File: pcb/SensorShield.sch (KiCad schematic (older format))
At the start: 51 parts, among them U14 ICE40UP5K-SG48ITR, U15 W25Q32JVSSIM

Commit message: stepper planes
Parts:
- removed R2: JUMPER, vs:ShortedJumper-2_P1.3mm_Bridged_Pad1.0x1.0mm, symbol UPduino_v3.0:Device_R
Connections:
- wire segments 327 -> 326
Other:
- note removed: "Core current \nmeasurement"
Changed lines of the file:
@@
 Wire Wire Line
 	2850 1900 3550 1900
-Text Label 4100 8350 0    50   ~ 0
+Text Label 4550 8350 2    50   ~ 0
 FLASH_MISO
 Text Label 5750 8550 0    50   ~ 0
@@
 Text Label 5750 8650 0    50   ~ 0
 IOB_25B_G3
-Text Label 4100 8250 0    50   ~ 0
+Text Label 4550 8250 2    50   ~ 0
 FLASH_MOSI
 $Comp
@@
 $EndComp
 $Comp
-L UPduino_v3.0:Device_R R?
-U 1 1 5E9D8BAA
-P 1100 6300
-AR Path="/5E9B245C/5E9D8BAA" Ref="R?"  Part="1"
-AR Path="/5E98CC69/5E9ECB99/5E9D8BAA" Ref="R2"  Part="1"
-AR Path="/5E9C016D/5E9D8BAA" Ref="R2"  Part="1"
-F 0 "R2" V 893 6300 50  0000 C CNN
-F 1 "JUMPER" V 984 6300 50  0000 C CNN
-F 2 "vs:ShortedJumper-2_P1.3mm_Bridged_Pad1.0x1.0mm" V 1030 6300 50  0001 C CNN
-F 3 "~" H 1100 6300 50  0001 C CNN
-	1    1100 6300
-	0    1    1    0
-$EndComp
-$Comp
 L UPduino_v3.0:power_+1V2 #PWR?
 U 1 1 5E9D8BB0
-P 850 6300
+P 1150 6300
 AR Path="/5E9B245C/5E9D8BB0" Ref="#PWR?"  Part="1"
 AR Path="/5E98CC69/5E9ECB99/5E9D8BB0" Ref="#PWR01"  Part="1"
 AR Path="/5E9C016D/5E9D8BB0" Ref="#PWR01"  Part="1"
-F 0 "#PWR01" H 850 6150 50  0001 C CNN
-F 1 "+1V2" H 865 6473 50  0000 C CNN
-F 2 "" H 850 6300 50  0001 C CNN
-F 3 "" H 850 6300 50  0001 C CNN
-	1    850  6300
+F 0 "#PWR01" H 1150 6150 50  0001 C CNN
+F 1 "+1V2" H 1165 6473 50  0000 C CNN
+F 2 "" H 1150 6300 50  0001 C CNN
+F 3 "" H 1150 6300 50  0001 C CNN
+	1    1150 6300
 	1    0    0    -1
 $EndComp
 Wire Wire Line
-	850  6300 950  6300
-Wire Wire Line
-	1250 6300 1400 6300
-Wire Wire Line
 	1700 1850 1700 1950
 Connection ~ 1700 1950
@@
 	1    0    0    -1
 $EndComp
-Text Notes 800  6550 0    50   ~ 0
-Core current \nmeasurement
 Connection ~ 6200 1950
 $Comp
@@
 Text HLabel 8900 8150 2    50   Output ~ 0
 ANALOG_[0..8]
+Wire Wire Line
+	1150 6300 1400 6300
 Wire Bus Line
 	8800 8150 8800 9000

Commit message: added ice40 regulators
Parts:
- removed R37, R38: JUMPER, vs:SolderJumper-2_0603_Open_TrianglePad1.0x1.5mm, symbol UPduino_v3.0:Device_R
- removed U15: W25Q32JVSSIM, Package_SO:SOIC-8_5.23x5.23mm_P1.27mm, symbol UPduino_v3.0:W25Q32JVSS-Memory_Flash
- added U?: GD25Q32CTIGR-Memory_Flash, Package_SO:SOIC-8_3.9x4.9mm_P1.27mm, symbol UPduino_v3.0:GD25Q32CTIGR-Memory_Flash
- U14: DigiKey (none) -> 220-2212-1-ND
- U14: DIgiKey (none) -> 220-2212-1-ND
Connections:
- net labels removed: IOB_18A, IOB_25B_G3
- wire segments 326 -> 321
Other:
- note removed: "Install 0 Ohms for qSPI"
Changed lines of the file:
@@
 EESchema Schematic File Version 4
-LIBS:keep_breathing_ctrl-cache
 EELAYER 30 0
 EELAYER END
@@
 F 2 "Package_DFN_QFN:QFN-48-1EP_7x7mm_P0.5mm_EP5.6x5.6mm" H 1700 1800 50  0001 C CNN
 F 3 "" H 1300 4150 50  0001 C CNN
+F 4 "220-2212-1-ND" H 1700 3150 50  0001 C CNN "DigiKey"
 	1    1700 3150
 	1    0    0    -1
@@
 F 1 "ICE40UP5K-SG48ITR" H 5900 2000 50  0000 L CNN
 F 2 "Package_DFN_QFN:QFN-48-1EP_7x7mm_P0.5mm_EP5.6x5.6mm" H 6200 1400 50  0001 C CNN
-F 3 "http://www.latticesemi.com/Products/FPGAandCPLD/iCE40Ultra" H 5800 3750 50  0001 C CNN
+F 3 "" H 5800 3750 50  0001 C CNN
+F 4 "220-2212-1-ND" H 6200 2750 50  0001 C CNN "DIgiKey"
 	3    6200 2750
 	1    0    0    -1
@@
 F 2 "Package_DFN_QFN:QFN-48-1EP_7x7mm_P0.5mm_EP5.6x5.6mm" H 1900 4250 50  0001 C CNN
 F 3 "" H 1500 6600 50  0001 C CNN
+F 4 "220-2212-1-ND" V 1900 5600 50  0001 C CNN "DIgiKey"
 	4    1900 5600
 	0    -1   -1   0
@@
 CRESET_N
 $Comp
-L UPduino_v3.0:W25Q32JVSS-Memory_Flash U?
-U 1 1 5E9D8AB7
-P 3550 8450
-AR Path="/5E9B245C/5E9D8AB7" Ref="U?"  Part="1"
-AR Path="/5E98CC69/5E9ECB99/5E9D8AB7" Ref="U15"  Part="1"
-AR Path="/5E9C016D/5E9D8AB7" Ref="U15"  Part="1"
-F 0 "U15" H 3700 8950 50  0000 C CNN
-F 1 "W25Q32JVSSIM" H 3900 8850 50  0000 C CNN
-F 2 "Package_SO:SOIC-8_5.23x5.23mm_P1.27mm" H 3550 8450 50  0001 C CNN
-F 3 "http://www.winbond.com/resource-files/w25q32jv%20revg%2003272018%20plus.pdf" H 3550 8450 50  0001 C CNN
-	1    3550 8450
-	1    0    0    -1
-$EndComp
-$Comp
 L UPduino_v3.0:power_GND #PWR?
 U 1 1 5E9D8ABD
-P 3550 8900
+P 3450 8850
 AR Path="/5E9B245C/5E9D8ABD" Ref="#PWR?"  Part="1"
 AR Path="/5E98CC69/5E9ECB99/5E9D8ABD" Ref="#PWR024"  Part="1"
 AR Path="/5E9C016D/5E9D8ABD" Ref="#PWR024"  Part="1"
-F 0 "#PWR024" H 3550 8650 50  0001 C CNN
-F 1 "GND" H 3555 8727 50  0000 C CNN
-F 2 "" H 3550 8900 50  0001 C CNN
-F 3 "" H 3550 8900 50  0001 C CNN
-	1    3550 8900
+F 0 "#PWR024" H 3450 8600 50  0001 C CNN
+F 1 "GND" H 3455 8677 50  0000 C CNN
+F 2 "" H 3450 8850 50  0001 C CNN
+F 3 "" H 3450 8850 50  0001 C CNN
+	1    3450 8850
 	1    0    0    -1
 $EndComp
@@
 Wire Wire Line
 	3550 7950 3550 8050
-Wire Wire Line
-	3550 8850 3550 8900
 $Comp
 L UPduino_v3.0:Device_C C?
@@
 Text Label 4550 8350 2    50   ~ 0
 FLASH_MISO
-Text Label 5750 8550 0    50   ~ 0
-IOB_18A
-Text Label 5750 8650 0    50   ~ 0
-IOB_25B_G3
 Text Label 4550 8250 2    50   ~ 0
 FLASH_MOSI
@@
 Text Notes 3100 1600 0    100  ~ 20
 FPGA Banks
-$Comp
-L UPduino_v3.0:Device_R R?
-U 1 1 5E9D8B7E
-P 5400 8550
-AR Path="/5E9B245C/5E9D8B7E" Ref="R?"  Part="1"
-AR Path="/5E98CC69/5E9ECB99/5E9D8B7E" Ref="R37"  Part="1"
-AR Path="/5E9C016D/5E9D8B7E" Ref="R37"  Part="1"
-F 0 "R37" V 5607 8550 50  0000 C CNN
-F 1 "JUMPER" V 5516 8550 50  0000 C CNN
-F 2 "vs:SolderJumper-2_0603_Open_TrianglePad1.0x1.5mm" V 5330 8550 50  0001 C CNN
-F 3 "~" H 5400 8550 50  0001 C CNN
-	1    5400 8550
-	0    -1   -1   0
-$EndComp
-$Comp
-L UPduino_v3.0:Device_R R?
-U 1 1 5E9D8B84
-P 5400 8650
-AR Path="/5E9B245C/5E9D8B84" Ref="R?"  Part="1"
-AR Path="/5E98CC69/5E9ECB99/5E9D8B84" Ref="R38"  Part="1"
-AR Path="/5E9C016D/5E9D8B84" Ref="R38"  Part="1"
-F 0 "R38" V 5200 8650 50  0000 C CNN
-F 1 "JUMPER" V 5300 8650 50  0000 C CNN
-F 2 "vs:SolderJumper-2_0603_Open_TrianglePad1.0x1.5mm" V 5330 8650 50  0001 C CNN
-F 3 "~" H 5400 8650 50  0001 C CNN
-	1    5400 8650
-	0    -1   -1   0
-$EndComp
-Wire Wire Line
-	4800 8550 5250 8550
-Connection ~ 4800 8550
-Wire Wire Line
-	5100 8650 5250 8650
-Connection ~ 5100 8650
-Wire Wire Line
-	5550 8650 5750 8650
-Wire Wire Line
-	5550 8550 5750 8550
 Text Notes 1250 2050 0    50   ~ 10
 Bank 0
@@
 $EndComp
 Connection ~ 6700 1950
-Text Notes 5050 9000 0    50   ~ 0
-Install 0 Ohms for qSPI
 Wire Wire Line
 	1200 5700 1500 5700
@@
 F 2 "Package_DFN_QFN:QFN-48-1EP_7x7mm_P0.5mm_EP5.6x5.6mm" H 3550 1800 50  0001 C CNN
 F 3 "" H 3150 4150 50  0001 C CNN
+F 4 "220-2212-1-ND" H 3550 3150 50  0001 C CNN "DigiKey"
 	2    3550 3150
 	1    0    0    -1
@@
 Wire Wire Line
 	1150 6300 1400 6300
+$Comp
+L UPduino_v3.0:GD25Q32CTIGR-Memory_Flash U?
+U 1 1 5EA7BA0C
+P 3550 8450
+F 0 "U?" H 3200 8100 50  0000 C CNN
+F 1 "GD25Q32CTIGR-Memory_Flash" H 3750 8850 50  0000 C CNN
+F 2 "Package_SO:SOIC-8_3.9x4.9mm_P1.27mm" H 3550 8450 50  0001 C CNN
+F 3 "http://www.gigadevice.com/datasheet/gd25q32c/" H 3550 8450 50  0001 C CNN
+F 4 "1970-1012-1-ND" H 3550 8450 50  0001 C CNN "DIgiKey"
+	1    3550 8450
+	1    0    0    -1
+$EndComp
 Wire Bus Line
 	8800 8150 8800 9000

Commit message: SPI connections between FPGA, PI and FLASH
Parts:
- added R5: 10K, Resistor_SMD:R_0603_1608Metric, symbol UPduino_v3.0:Device_R
- gave numbers to parts that had none: 1
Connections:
- net labels added: 1V2_ICE, 3V3_ICE, SPI_ICE0, SPI_ICE1, SPI_ICE2, SPI_ICE3, SPI_ICE4, SPI_ICE[0..4]
- net labels removed: +1V2, +3.3V, FLASH_MISO, FLASH_MOSI
- wire segments 321 -> 327
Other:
- note added: "Pull down\nFPGA as Slave"
- note added: "Pull up\nFPGA as Master"
- moved on the sheet: C45, R29, R33, R34

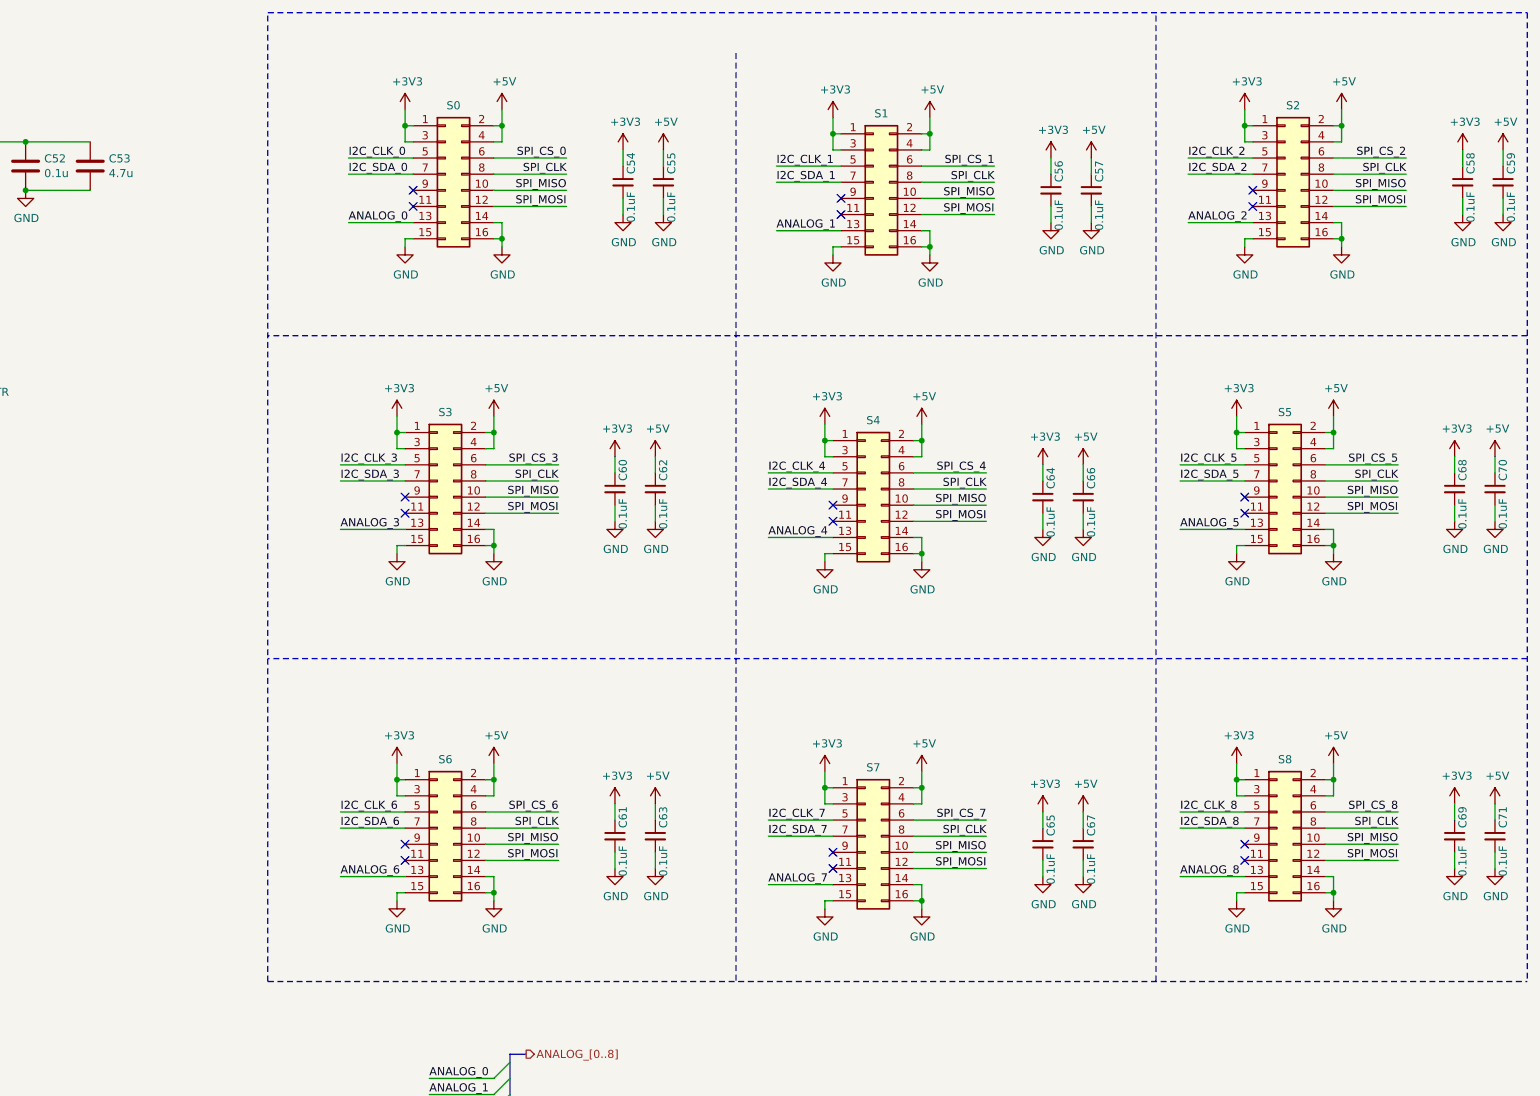
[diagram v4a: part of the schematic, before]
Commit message: support connectors
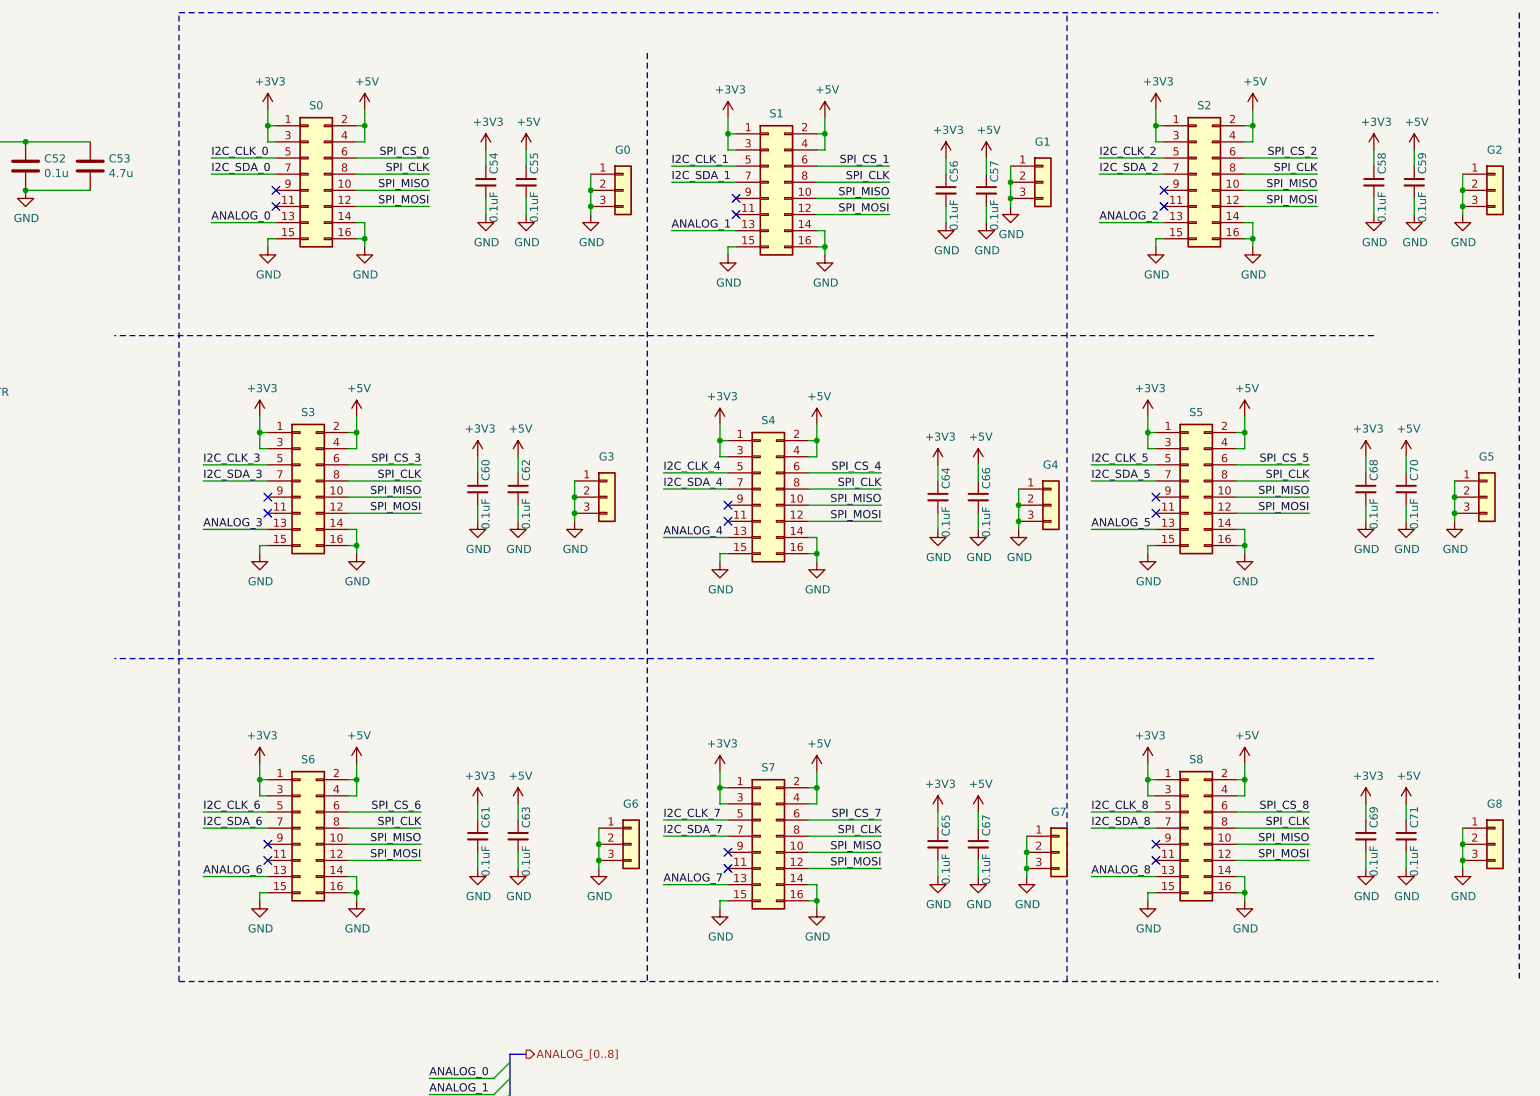
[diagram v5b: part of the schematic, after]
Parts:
- added G0, G1, G2, G3, G4, G5, G6, G7, G8: Conn_01x03, Connector_PinSocket_2.54mm:PinSocket_1x03_P2.54mm_Vertical_SMD_Pin1Right, symbol Connector_Generic:Conn_01x03
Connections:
- net GND: now also G0.1 (Pin_1), G0.2 (Pin_2), G0.3 (Pin_3), G1.1 (Pin_1), G1.2 (Pin_2), G1.3 (Pin_3), G2.1 (Pin_1), G2.2 (Pin_2), G2.3 (Pin_3), G3.1 (Pin_1), G3.2 (Pin_2), G3.3 (Pin_3), G4.1 (Pin_1), G4.2 (Pin_2), G4.3 (Pin_3), G5.1 (Pin_1), G5.2 (Pin_2), G5.3 (Pin_3), G6.1 (Pin_1), G6.2 (Pin_2), G6.3 (Pin_3), G7.1 (Pin_1), G7.2 (Pin_2), G7.3 (Pin_3), G8.1 (Pin_1), G8.2 (Pin_2), G8.3 (Pin_3)
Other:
- moved on the sheet: C54, C55, C56, C57, C58, C59, C60, C61, C62, C63, C64, C65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

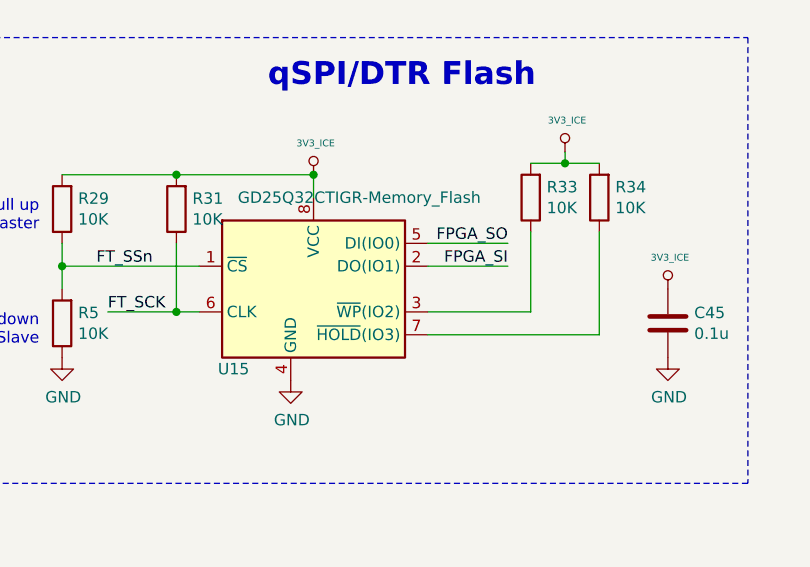
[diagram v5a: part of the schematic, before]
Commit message: spi flash placement
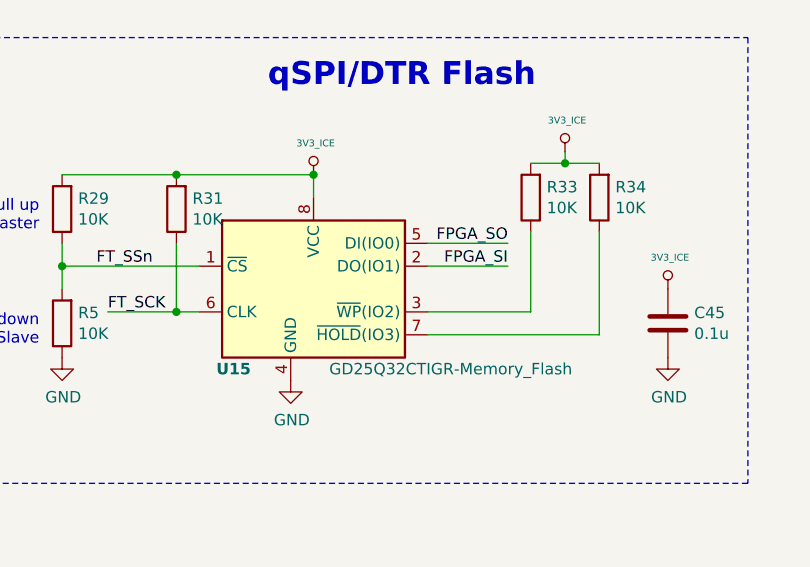
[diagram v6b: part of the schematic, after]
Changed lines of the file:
@@
 U 1 1 5EA7BA0C
 P 3550 8450
-F 0 "U15" H 3200 8100 50  0000 C CNN
-F 1 "GD25Q32CTIGR-Memory_Flash" H 3750 8850 50  0000 C CNN
+F 0 "U15" H 3200 8100 50  0000 C CNB
+F 1 "GD25Q32CTIGR-Memory_Flash" H 4150 8100 50  0000 C CNN
 F 2 "Package_SO:SOIC-8_3.9x4.9mm_P1.27mm" H 3550 8450 50  0001 C CNN
 F 3 "http://www.gigadevice.com/datasheet/gd25q32c/" H 3550 8450 50  0001 C CNN

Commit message: improving shield stability
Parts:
- G0, G1, G2, G3, G4, G5, G6, G7, G8: footprint Connector_PinSocket_2.54mm:PinSocket_1x03_P2.54mm_Vertical_SMD_Pin1Right -> Connector_PinSocket_2.54mm:PinSocket_2x05_P2.54mm_Vertical_SMD; symbol Connector_Generic:Conn_01x03 -> Connector_Generic:Conn_02x05_Odd_Even
- S0, S1, S2, S3, S4, S5, S6, S7, S8: value Conn_02x08_Counter_Clockwise -> Conn_02x07_Counter_Clockwise; footprint Connector_PinSocket_2.54mm:PinSocket_2x08_P2.54mm_Vertical_SMD -> Connector_PinSocket_2.54mm:PinSocket_2x07_P2.54mm_Vertical_SMD; symbol Connector_Generic:Conn_02x08_Odd_Even -> Connector_Generic:Conn_02x07_Odd_Even
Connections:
- net ANALOG_0: now also S0.9 (Pin_9); no longer S0.13 (Pin_13)
- net ANALOG_3: now also S3.9 (Pin_9); no longer S3.13 (Pin_13)
- net ANALOG_6: now also S6.9 (Pin_9); no longer S6.13 (Pin_13)
- net GND: now also G0.10 (Pin_10), G0.4 (Pin_4), G0.5 (Pin_5), G0.6 (Pin_6), G0.7 (Pin_7), G0.8 (Pin_8), G0.9 (Pin_9), G1.10 (Pin_10), G1.4 (Pin_4), G1.5 (Pin_5), G1.6 (Pin_6), G1.7 (Pin_7), G1.8 (Pin_8), G1.9 (Pin_9), G2.10 (Pin_10), G2.4 (Pin_4), G2.5 (Pin_5), G2.6 (Pin_6), G2.7 (Pin_7), G2.8 (Pin_8), G2.9 (Pin_9), G3.10 (Pin_10), G3.4 (Pin_4), G3.5 (Pin_5), G3.6 (Pin_6), G3.7 (Pin_7), G3.8 (Pin_8), G3.9 (Pin_9), G4.10 (Pin_10), G4.4 (Pin_4), G4.5 (Pin_5), G4.6 (Pin_6), G4.7 (Pin_7), G4.8 (Pin_8), G4.9 (Pin_9), G5.10 (Pin_10), G5.4 (Pin_4), G5.5 (Pin_5), G5.6 (Pin_6), G5.7 (Pin_7), G5.8 (Pin_8), G5.9 (Pin_9), G6.10 (Pin_10), G6.4 (Pin_4), G6.5 (Pin_5), G6.6 (Pin_6), G6.7 (Pin_7), G6.8 (Pin_8), G6.9 (Pin_9), G7.10 (Pin_10), G7.4 (Pin_4), G7.5 (Pin_5), G7.6 (Pin_6), G7.7 (Pin_7), G7.8 (Pin_8), G7.9 (Pin_9), G8.10 (Pin_10), G8.4 (Pin_4), G8.5 (Pin_5), G8.6 (Pin_6), G8.7 (Pin_7), G8.8 (Pin_8), G8.9 (Pin_9), S0.11 (Pin_11), S0.13 (Pin_13), S3.11 (Pin_11), S3.13 (Pin_13), S6.11 (Pin_11), S6.13 (Pin_13); no longer S0.15 (Pin_15), S0.16 (Pin_16), S1.15 (Pin_15), S1.16 (Pin_16), S2.15 (Pin_15), S2.16 (Pin_16), S3.15 (Pin_15), S3.16 (Pin_16), S4.15 (Pin_15), S4.16 (Pin_16), S5.15 (Pin_15), S5.16 (Pin_16), S6.15 (Pin_15), S6.16 (Pin_16), S7.15 (Pin_15), S7.16 (Pin_16), S8.15 (Pin_15), S8.16 (Pin_16)
- no-connect marks 18 -> 12
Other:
- moved on the sheet: C54, C55, C56, C57, C58, C59, C60, C61, C62, C63, C64, C65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
